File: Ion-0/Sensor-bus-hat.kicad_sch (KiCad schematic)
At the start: 89 parts, among them J10 Conn_Heater, J11 Conn_01x02, J12 Conn_01x02, J13 Conn_01x04, J6 Coaxial_Small, J7 Conn_01x02, J8 Conn_Heater, J9 Conn_Heater, Q1 IRLML6244, Q2 IRLML6244, Q3 IRLML6244, Q4 IRLML6244, U1 MS860702BA01-50, U2 LMT84DCK, U3 BNO085, U4 TCA9617ADGKR, U5 LMT84DCK, U6 TPS3850H50DRCR, U7 MAX-M10M-00B, U8 SN65HVD230, Y1 9HT10-32.768KBZF-T

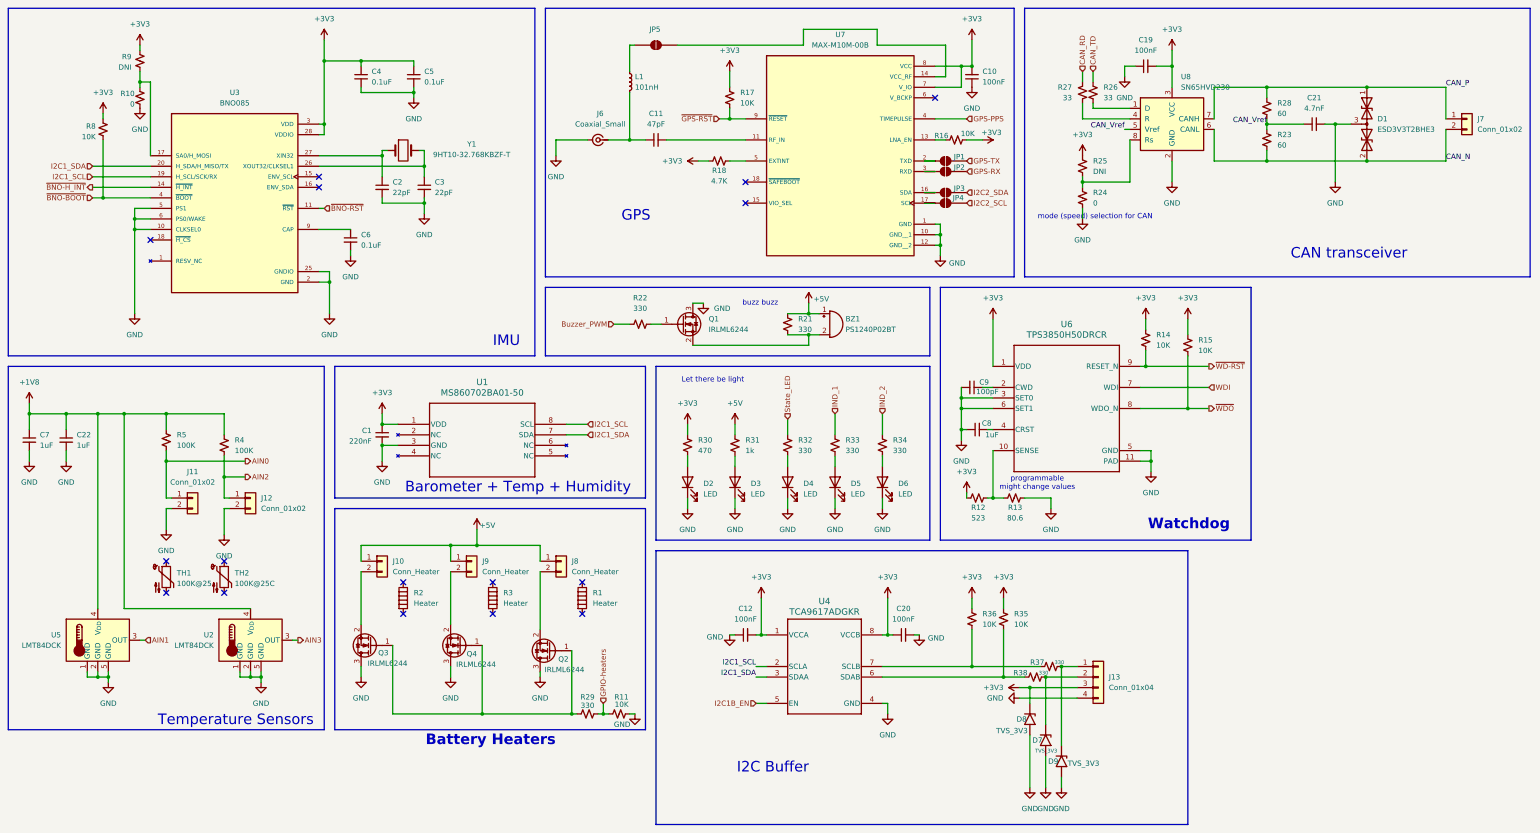
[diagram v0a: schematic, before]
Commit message: Fixed symbol library
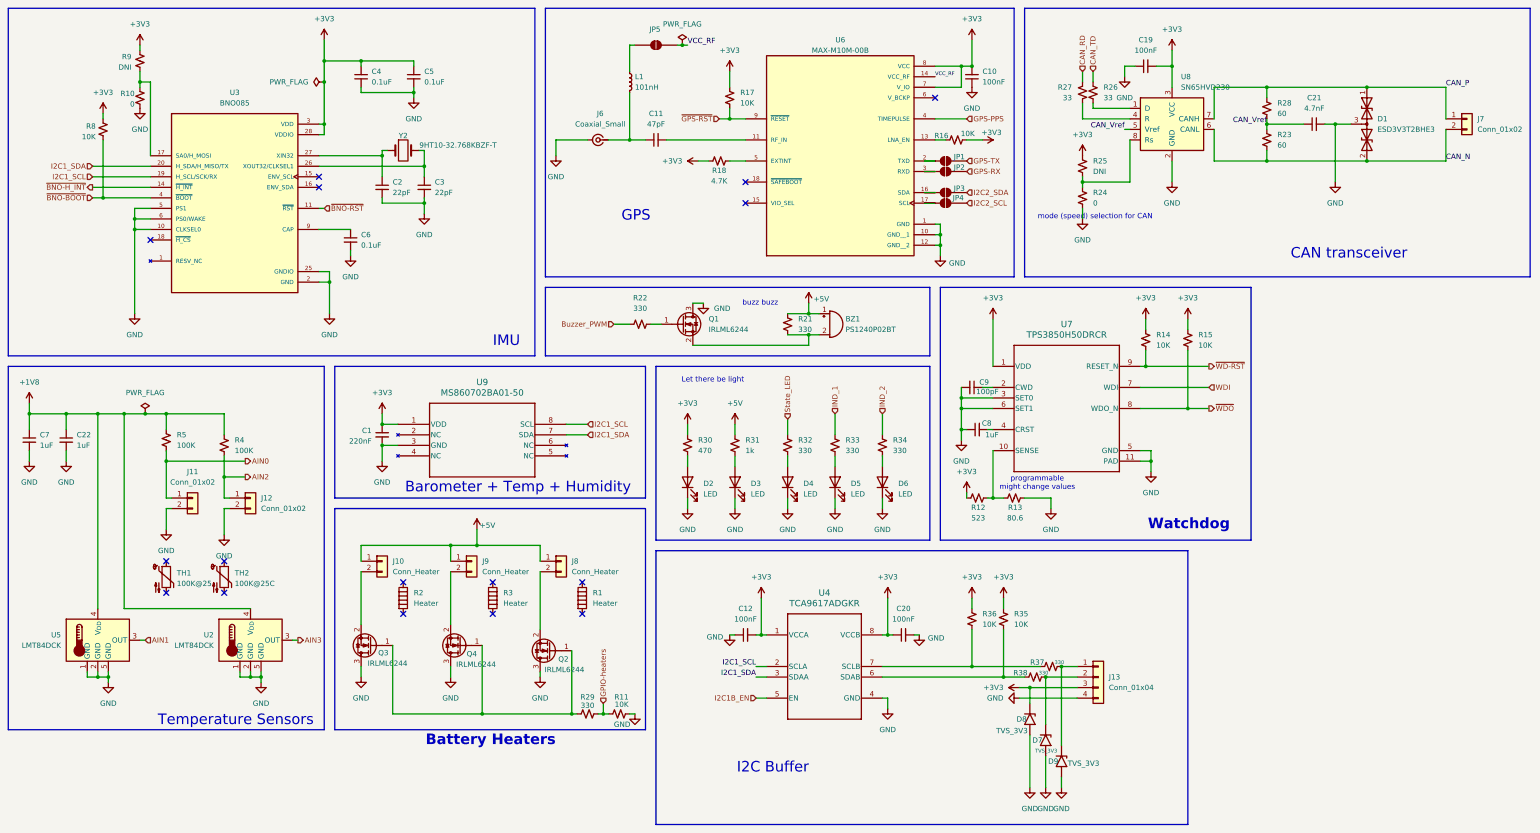
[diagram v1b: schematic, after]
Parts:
- removed U1: MS860702BA01-50, MS860702BA01-50_TEC, symbol MS8607:MS860702BA01-50
- removed U3: BNO085, BNO085:IC_BNO085, symbol BNO085:BNO085
- removed U4: TCA9617ADGKR, DGK0008A, symbol 2026-03-24_01-09-19:TCA9617ADGKR
- removed U6: TPS3850H50DRCR, DRC0010J, symbol MI-CHAB-library:TPS3850H50DRCR
- removed U7: MAX-M10M-00B, symbol MI-CHAB-library:MAX-M10M-00B
- removed Y1: 9HT10-32.768KBZF-T, symbol MI-CHAB-library:9HT10-32.768KBZF-T
- added U3: BNO085, BNO085:IC_BNO085, symbol 1_ion_library:BNO085
- added U4: TCA9617ADGKR, DGK0008A, symbol 1_ion_library:TCA9617ADGKR
- added U6: MAX-M10M-00B, MAX-M10M-00B:XCVR_MAX-M10M-00B, symbol 1_ion_library:MAX-M10M-00B
- added U7: TPS3850H50DRCR, DRC0010J, symbol 1_ion_library:TPS3850H50DRCR
- added U9: MS860702BA01-50, MS860702BA01-50_TEC, symbol 1_ion_library:MS860702BA01-50
- added Y2: 9HT10-32.768KBZF-T, symbol Device:Crystal
- J10, J11, J12, J7, J8, J9: footprint (none) -> Connector_JST:JST_EH_B2B-EH-A_1x02_P2.50mm_Vertical
- J13: footprint (none) -> Connector_JST:JST_EH_B4B-EH-A_1x04_P2.50mm_Vertical
- J6: footprint (none) -> Connector_Coaxial:SMA_Samtec_SMA-J-P-H-ST-EM1_EdgeMount
- JP1, JP2, JP3, JP4, JP5: footprint (none) -> Jumper:SolderJumper-2_P1.3mm_Open_TrianglePad1.0x1.5mm
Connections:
- net +3V3: now also U3.28 (VDDIO), U3.3 (VDD), U4.1 (VCCA), U4.8 (VCCB), U6.7 (V_IO), U6.8 (VCC), U7.1 (VDD), U9.1 (VDD)
- net GND: now also U3.10 (CLKSEL0), U3.2 (GND), U3.25 (GNDIO), U3.5 (PS1), U3.6 (PS0/WAKE), U4.4 (GND), U6.1 (GND), U6.10 (GND__1), U6.12 (GND__2), U7.11 (PAD), U7.3 (SET0), U7.5 (GND), U7.6 (SET1), U9.3 (GND)
- net GPS-PPS: now also U6.4 (TIMEPULSE)
- net I2C1B_EN: now also U4.5 (EN)
- net I2C1_SCL: now also U3.19 (H_SCL/SCK/RX), U4.2 (SCLA), U9.8 (SCL)
- net I2C1_SDA: now also U3.20 (H_SDA/H_MISO/TX), U4.3 (SDAA), U9.7 (SDA)
- net WDI: now also U7.7 (WDI)
- net ~{BNO-BOOT}: now also U3.4 (~{BOOT})
- net ~{BNO-H_INT}: now also U3.14 (~{H_INT})
- net ~{BNO-RST}: now also U3.11 (~{RST})
- net ~{GPS-RST}: now also U6.9 (~{RESET})
- net ~{WD-RST}: now also U7.9 (RESET_N)
- net ~{WDO}: now also U7.8 (WDO_N)
- net at C3.1: now also U3.26 (XOUT32/CLKSEL1), Y2.2
- net at R10.1, R9.2: now also U3.17 (SA0/H_MOSI)
- net at C2.1: now also U3.27 (XIN32), Y2.1
- net at C6.1: now also U3.9 (CAP)
- net at JP2.1 (A): now also U6.3 (RXD)
- net at C9.1: now also U7.2 (CWD)
- net at R35.2, R38.1: now also U4.6 (SDAB)
- net at R18.1: now also U6.5 (EXTINT)
- net at C11.2: now also U6.11 (RF_IN)
- net at C8.2: now also U7.4 (CRST)
- net at R12.2, R13.2: now also U7.10 (SENSE)
- net at R36.2, R37.1: now also U4.7 (SCLB)
- net at R16.1: now also U6.13 (LNA_EN)
- net VCC_RF: now reaches JP5.2 (B)
- net VCC_RF: now also U6.14 (VCC_RF)
- net at JP3.1 (A): now also U6.16 (SDA)
- net at JP4.1 (A): now also U6.17 (SCL)
- net at JP1.1 (A): now also U6.2 (TXD)
- new net: U3.1 (RESV_NC), U3.12 (RESV_NC), U3.13 (RESV_NC), U3.21 (RESV_NC), U3.22 (RESV_NC), U3.23 (RESV_NC), U3.24 (RESV_NC), U3.7 (RESV_NC), U3.8 (RESV_NC)
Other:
- moved on the sheet: R15

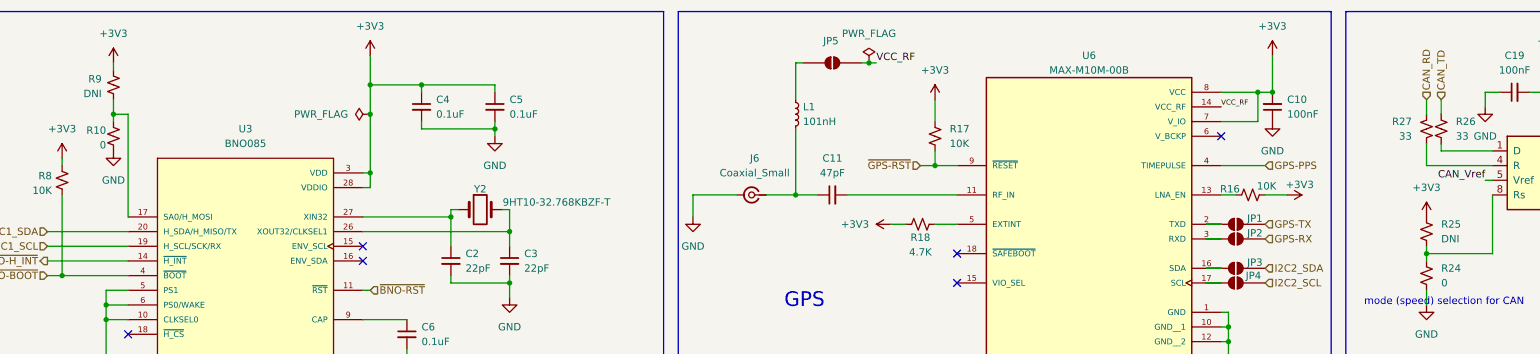
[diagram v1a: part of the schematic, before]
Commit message: library fix, no 3d models tho
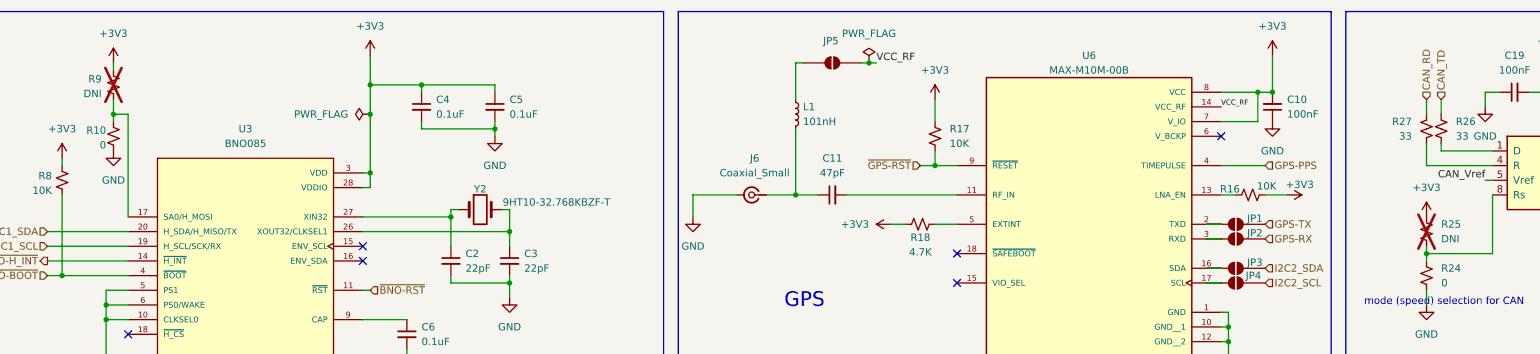
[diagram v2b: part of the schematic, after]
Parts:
- BZ1: footprint (none) -> Buzzer_Beeper:Buzzer_TDK_PS1240P02BT_D12.2mm_H6.5mm
- C1, C10, C11, C12, C19, C2, C20, C21, C22, C3, C4, C5, C6, C7, C8, C9: footprint (none) -> Capacitor_SMD:C_0201_0603Metric
- D2, D3, D4, D5, D6: footprint (none) -> LED_SMD:LED_0805_2012Metric
- J10, J11, J12, J7, J8, J9: footprint Connector_JST:JST_EH_B2B-EH-A_1x02_P2.50mm_Vertical -> Connector_JST:JST_SH_SM02B-SRSS-TB_1x02-1MP_P1.00mm_Horizontal
- J13: footprint Connector_JST:JST_EH_B4B-EH-A_1x04_P2.50mm_Vertical -> Connector_JST:JST_SH_SM04B-SRSS-TB_1x04-1MP_P1.00mm_Horizontal
- L1: footprint (none) -> Inductor_SMD:L_0402_1005Metric
- R10, R11, R12, R13, R14, R15, R16, R17, R18, R21, R22, R23, R24, R26, R27, R28, R29, R30, R31, R32, R33, R34, R35, R36, R37, R38, R4, R5, R8: footprint (none) -> Resistor_SMD:R_0603_1608Metric_Pad0.98x0.95mm_HandSolder
- R25, R9: footprint (none) -> Resistor_SMD:R_0603_1608Metric_Pad0.98x0.95mm_HandSolder; now not fitted
- U3: footprint BNO085:IC_BNO085 -> 1_Ion:IC_BNO085
- U4: footprint DGK0008A -> 1_Ion:TCA9617A
- U6: footprint MAX-M10M-00B:XCVR_MAX-M10M-00B -> 1_Ion:XCVR_MAX-M10M-00B
- U7: footprint DRC0010J -> 1_Ion:TPS3850
- U9: footprint MS860702BA01-50_TEC -> 1_Ion:MS860702BA01-50_TEC
- Y2: footprint (none) -> Inductor_SMD:L_1206_3216Metric
